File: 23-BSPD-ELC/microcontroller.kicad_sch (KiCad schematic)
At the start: 57 parts, among them J2 Conn_01x02, J3 Conn_01x02, J4 SWD, SW2 SW_SPDT, U16 STM32F105RCTx, U17 SN65HVD230, U18 SN65HVD230, Y1 16MHz

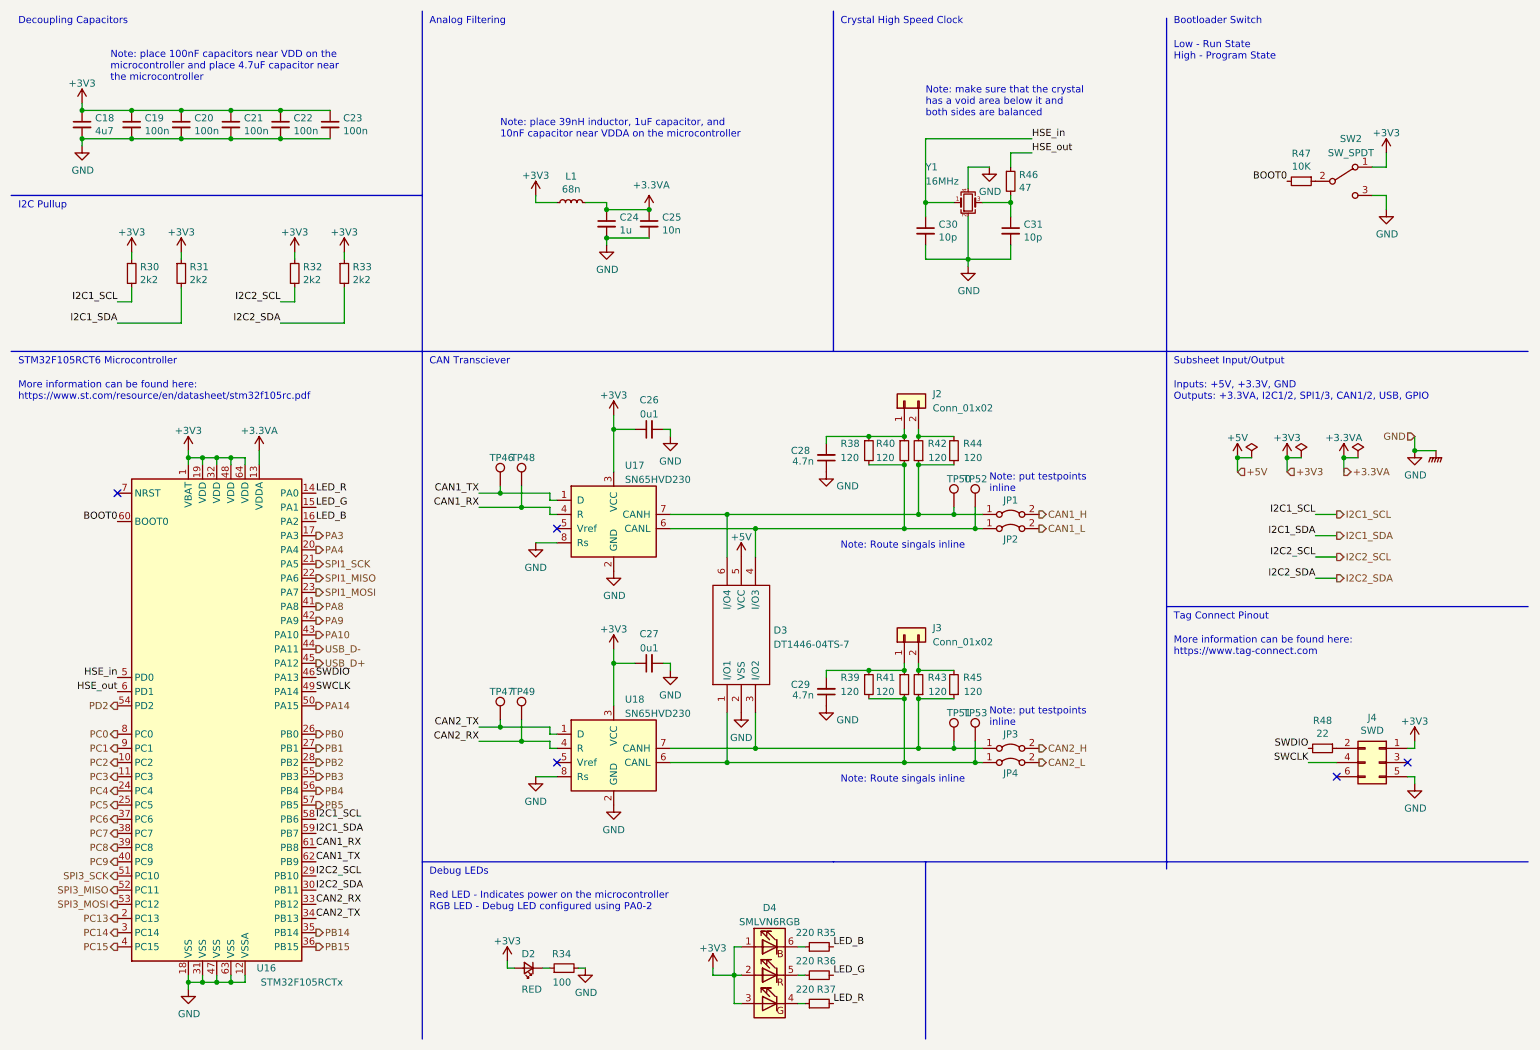
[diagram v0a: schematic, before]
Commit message: Revision changes and updates to some footprints
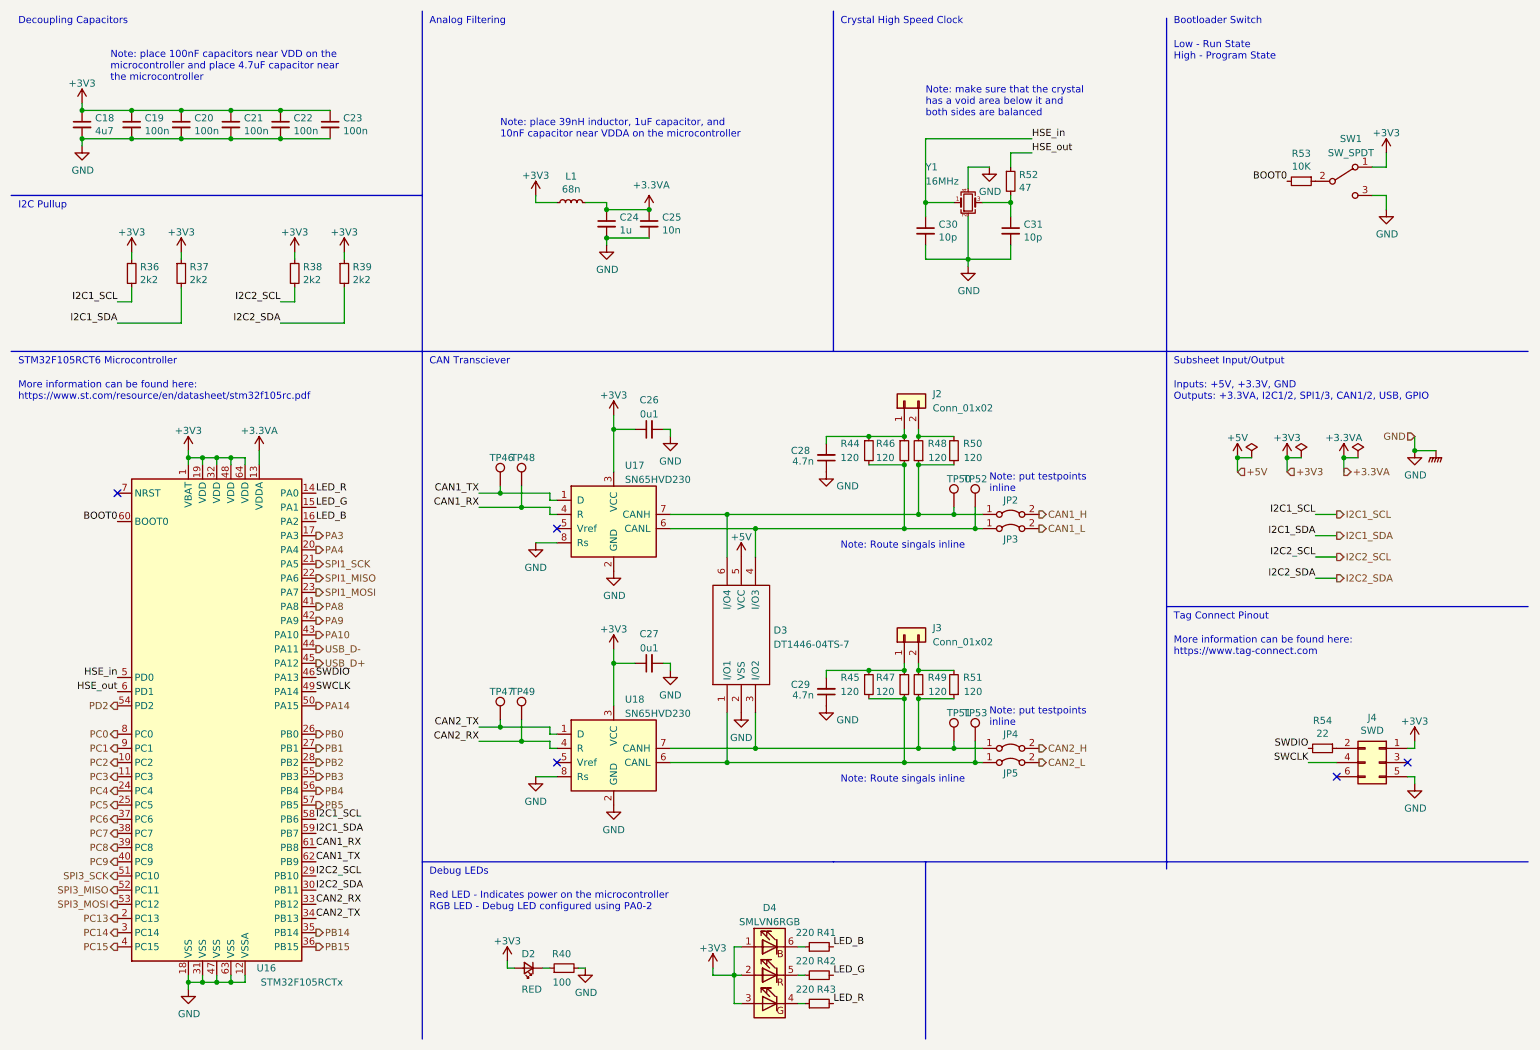
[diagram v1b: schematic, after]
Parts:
- renumbered JP1 to JP2, JP2 to JP3, JP3 to JP4, JP4 to JP5, R30 to R36, R31 to R37, R32 to R38, R33 to R39, R34 to R40, R35 to R41, R36 to R42, R37 to R43, R38 to R44, R39 to R45, R40 to R46, R41 to R47, R42 to R48, R43 to R49, R44 to R50, R45 to R51, R46 to R52, R47 to R53, R48 to R54, SW2 to SW1

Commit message: Updated pcb layout; Watchdog on board still in progress
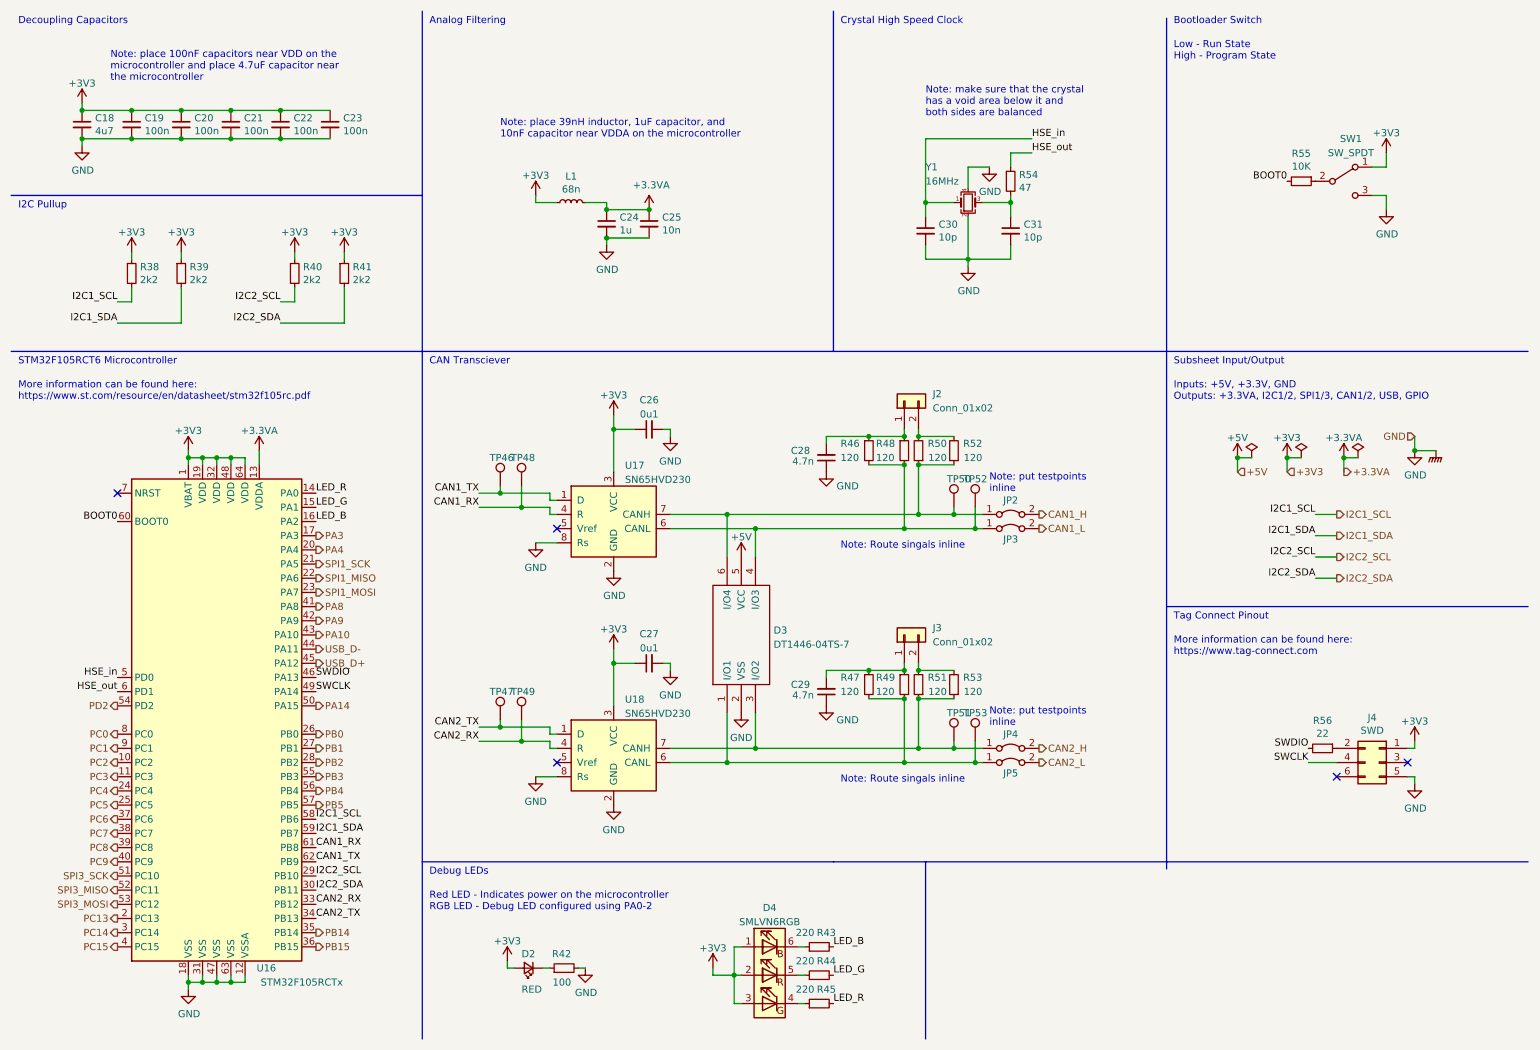
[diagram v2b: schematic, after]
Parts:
- renumbered R36 to R38, R37 to R39, R38 to R40, R39 to R41, R40 to R42, R41 to R43, R42 to R44, R43 to R45, R44 to R46, R45 to R47, R46 to R48, R47 to R49, R48 to R50, R49 to R51, R50 to R52, R51 to R53, R52 to R54, R53 to R55, R54 to R56
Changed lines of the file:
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@@
   (symbol (lib_id "Device:R_Small") (at 243.84 43.18 270) (unit 1)
     (in_bom yes) (on_board yes)
-    (property "Reference" "R53" (id 0) (at 243.84 38.2016 90))
+    (property "Reference" "R55" (id 0) (at 243.84 38.2016 90))
     (property "Value" "10K" (id 1) (at 243.84 40.513 90))
     (property "Footprint" "Resistor_SMD:R_0603_1608Metric" (id 2) (at 243.84 43.18 0)
@@
   (symbol (lib_id "Device:R_Small") (at 191.77 43.18 0) (unit 1)
     (in_bom yes) (on_board yes)
-    (property "Reference" "R52" (id 0) (at 193.2686 42.0116 0)
+    (property "Reference" "R54" (id 0) (at 193.2686 42.0116 0)
       (effects (font (size 1.27 1.27)) (justify left))
     )
@@
   (symbol (lib_id "Device:R_Small") (at 111.76 184.15 90) (unit 1)
     (in_bom yes) (on_board yes)
-    (property "Reference" "R40" (id 0) (at 113.03 181.61 90)
+    (property "Reference" "R42" (id 0) (at 113.03 181.61 90)
       (effects (font (size 1.27 1.27)) (justify left))
     )
@@
   (symbol (lib_id "Device:R_Small") (at 247.65 144.78 270) (unit 1)
     (in_bom yes) (on_board yes)
-    (property "Reference" "R54" (id 0) (at 247.65 139.8016 90))
+    (property "Reference" "R56" (id 0) (at 247.65 139.8016 90))
     (property "Value" "22" (id 1) (at 247.65 142.113 90))
     (property "Footprint" "Resistor_SMD:R_0603_1608Metric" (id 2) (at 247.65 144.78 0)
@@
   (symbol (lib_id "Device:R_Small") (at 34.29 59.69 0) (unit 1)
     (in_bom yes) (on_board yes)
-    (property "Reference" "R36" (id 0) (at 35.7886 58.5216 0)
+    (property "Reference" "R38" (id 0) (at 35.7886 58.5216 0)
       (effects (font (size 1.27 1.27)) (justify left))
     )
@@
   (symbol (lib_id "Device:R_Small") (at 43.18 59.69 0) (unit 1)
     (in_bom yes) (on_board yes)
-    (property "Reference" "R37" (id 0) (at 44.6786 58.5216 0)
+    (property "Reference" "R39" (id 0) (at 44.6786 58.5216 0)
       (effects (font (size 1.27 1.27)) (justify left))
     )
@@
   (symbol (lib_id "Device:R_Small") (at 63.5 59.69 0) (unit 1)
     (in_bom yes) (on_board yes)
-    (property "Reference" "R38" (id 0) (at 64.9986 58.5216 0)
+    (property "Reference" "R40" (id 0) (at 64.9986 58.5216 0)
       (effects (font (size 1.27 1.27)) (justify left))
     )
@@
   (symbol (lib_id "Device:R_Small") (at 72.39 59.69 0) (unit 1)
     (in_bom yes) (on_board yes)
-    (property "Reference" "R39" (id 0) (at 73.8886 58.5216 0)
+    (property "Reference" "R41" (id 0) (at 73.8886 58.5216 0)
       (effects (font (size 1.27 1.27)) (justify left))
     )
@@
   (symbol (lib_id "Device:R_Small") (at 157.48 190.5 90) (unit 1)
     (in_bom yes) (on_board yes)
-    (property "Reference" "R43" (id 0) (at 158.75 187.96 90))
+    (property "Reference" "R45" (id 0) (at 158.75 187.96 90))
     (property "Value" "220" (id 1) (at 154.94 187.96 90))
     (property "Footprint" "Resistor_SMD:R_0603_1608Metric" (id 2) (at 157.48 190.5 0)
@@
   (symbol (lib_id "Device:R_Small") (at 172.72 133.35 0) (unit 1)
     (in_bom yes) (on_board yes)
-    (property "Reference" "R47" (id 0) (at 167.64 132.08 0)
+    (property "Reference" "R49" (id 0) (at 167.64 132.08 0)
       (effects (font (size 1.27 1.27)) (justify left))
     )
@@
   (symbol (lib_id "Device:R_Small") (at 157.48 185.42 90) (unit 1)
     (in_bom yes) (on_board yes)
-    (property "Reference" "R42" (id 0) (at 158.75 182.88 90))
+    (property "Reference" "R44" (id 0) (at 158.75 182.88 90))
     (property "Value" "220" (id 1) (at 154.94 182.88 90))
     (property "Footprint" "Resistor_SMD:R_0603_1608Metric" (id 2) (at 157.48 185.42 0)
@@
   (symbol (lib_id "Device:R_Small") (at 181.61 133.35 180) (unit 1)
     (in_bom yes) (on_board yes)
-    (property "Reference" "R51" (id 0) (at 186.69 132.08 0)
+    (property "Reference" "R53" (id 0) (at 186.69 132.08 0)
       (effects (font (size 1.27 1.27)) (justify left))
     )
@@
   (symbol (lib_id "Device:R_Small") (at 157.48 180.34 90) (unit 1)
     (in_bom yes) (on_board yes)
-    (property "Reference" "R41" (id 0) (at 158.75 177.8 90))
+    (property "Reference" "R43" (id 0) (at 158.75 177.8 90))
     (property "Value" "220" (id 1) (at 154.94 177.8 90))
     (property "Footprint" "Resistor_SMD:R_0603_1608Metric" (id 2) (at 157.48 180.34 0)
@@
   (symbol (lib_id "Device:R_Small") (at 175.26 133.35 180) (unit 1)
     (in_bom yes) (on_board yes)
-    (property "Reference" "R49" (id 0) (at 180.34 132.08 0)
+    (property "Reference" "R51" (id 0) (at 180.34 132.08 0)
       (effects (font (size 1.27 1.27)) (justify left))
     )
@@
   (symbol (lib_id "Device:R_Small") (at 166.37 133.35 0) (unit 1)
     (in_bom yes) (on_board yes)
-    (property "Reference" "R45" (id 0) (at 161.29 132.08 0)
+    (property "Reference" "R47" (id 0) (at 161.29 132.08 0)
       (effects (font (size 1.27 1.27)) (justify left))
     )
@@
   (symbol (lib_id "Device:R_Small") (at 181.61 91.44 180) (unit 1)
     (in_bom yes) (on_board yes)
-    (property "Reference" "R50" (id 0) (at 186.69 90.17 0)
+    (property "Reference" "R52" (id 0) (at 186.69 90.17 0)
       (effects (font (size 1.27 1.27)) (justify left))
     )
@@
   (symbol (lib_id "Device:R_Small") (at 172.72 91.44 0) (unit 1)
     (in_bom yes) (on_board yes)
-    (property "Reference" "R46" (id 0) (at 167.64 90.17 0)
+    (property "Reference" "R48" (id 0) (at 167.64 90.17 0)
       (effects (font (size 1.27 1.27)) (justify left))
     )
@@
   (symbol (lib_id "Device:R_Small") (at 166.37 91.44 0) (unit 1)
     (in_bom yes) (on_board yes)
-    (property "Reference" "R44" (id 0) (at 161.29 90.17 0)
+    (property "Reference" "R46" (id 0) (at 161.29 90.17 0)
       (effects (font (size 1.27 1.27)) (justify left))
     )
@@
   (symbol (lib_id "Device:R_Small") (at 175.26 91.44 180) (unit 1)
     (in_bom yes) (on_board yes)
-    (property "Reference" "R48" (id 0) (at 180.34 90.17 0)
-      (effects (font (size 1.27 1.27)) (justify left))
-    )
+    (property "Reference" "R50" (id 0) (at 180.34 90.17 0)
+      (effects (font (size 1.27 1.27)) (justify left))
+    )

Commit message: BSPD layout
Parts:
- removed C27: 0u1, Capacitor_SMD:C_0603_1608Metric, symbol Device:C_Small
- removed C29: 4.7n, Capacitor_SMD:C_0603_1608Metric, symbol Device:C_Small
- removed J3: Conn_01x02, Connector_PinHeader_2.54mm:PinHeader_1x02_P2.54mm_Vertical, symbol Connector_Generic:Conn_01x02
- removed JP4, JP5: (no value), Jumper:SolderJumper-2_P1.3mm_Bridged2Bar_Pad1.0x1.5mm, symbol Jumper:Jumper_2_Bridged
- removed R47, R49, R51, R53: 120, Resistor_SMD:R_0603_1608Metric, symbol Device:R_Small
- removed TP47, TP49, TP51, TP53: (no value), TestPoint:TestPoint_THTPad_1.0x1.0mm_Drill0.5mm, symbol Connector:TestPoint
- removed U18: SN65HVD230, Package_SO:SOIC-8_3.9x4.9mm_P1.27mm, symbol Interface_CAN_LIN:SN65HVD230
- J3: renamed from J4; footprint Connector_PinHeader_1.27mm:PinHeader_2x03_P1.27mm_Vertical -> Connector:Tag-Connect_TC2030-IDC-FP_2x03_P1.27mm_Vertical
- renumbered C28 to C27, C30 to C28, C31 to C29, R38 to R37, R39 to R38, R40 to R39, R41 to R40, R42 to R41, R43 to R42, R44 to R43, R45 to R44, R46 to R45, R48 to R46, R50 to R47, R52 to R48, R54 to R49, R55 to R50, R56 to R51, TP48 to TP47, TP50 to TP48, TP52 to TP49
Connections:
- net CAN2_RX: no longer names the net of U16.33 (PB12)
- net CAN2_TX: no longer names the net of U16.34 (PB13)
- no-connect marks 5 -> 8
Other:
- moved on the sheet: TP48
